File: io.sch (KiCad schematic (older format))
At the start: 2 parts

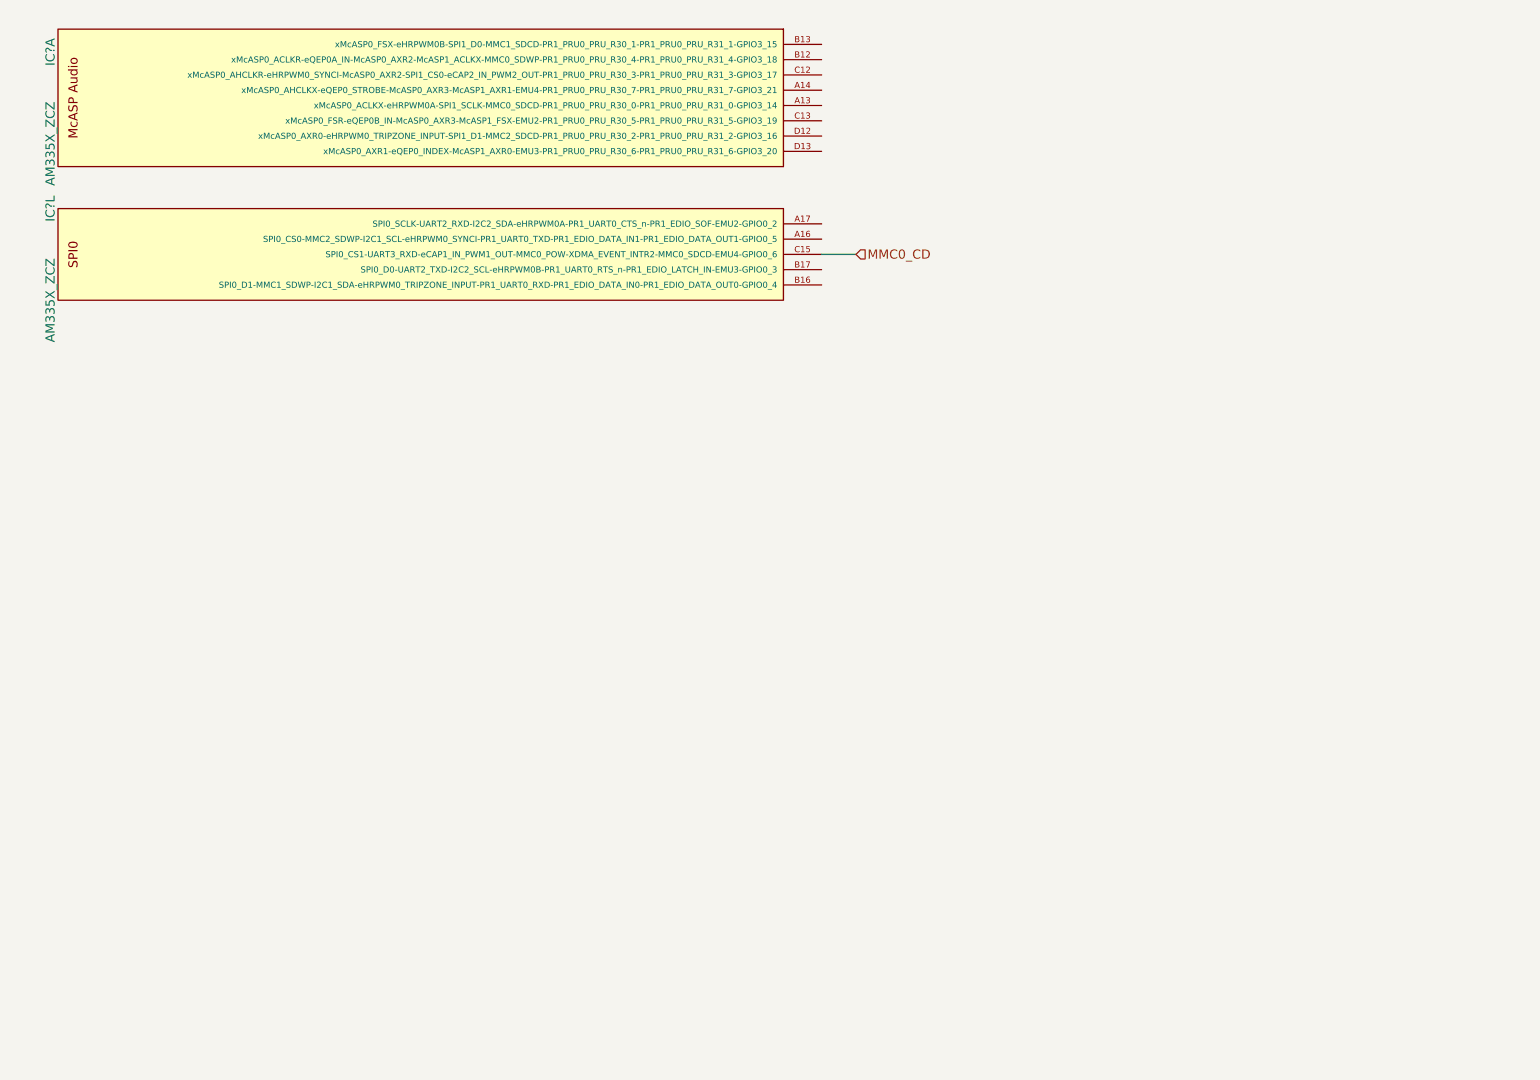
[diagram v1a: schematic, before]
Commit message: hierarchical sheets defined
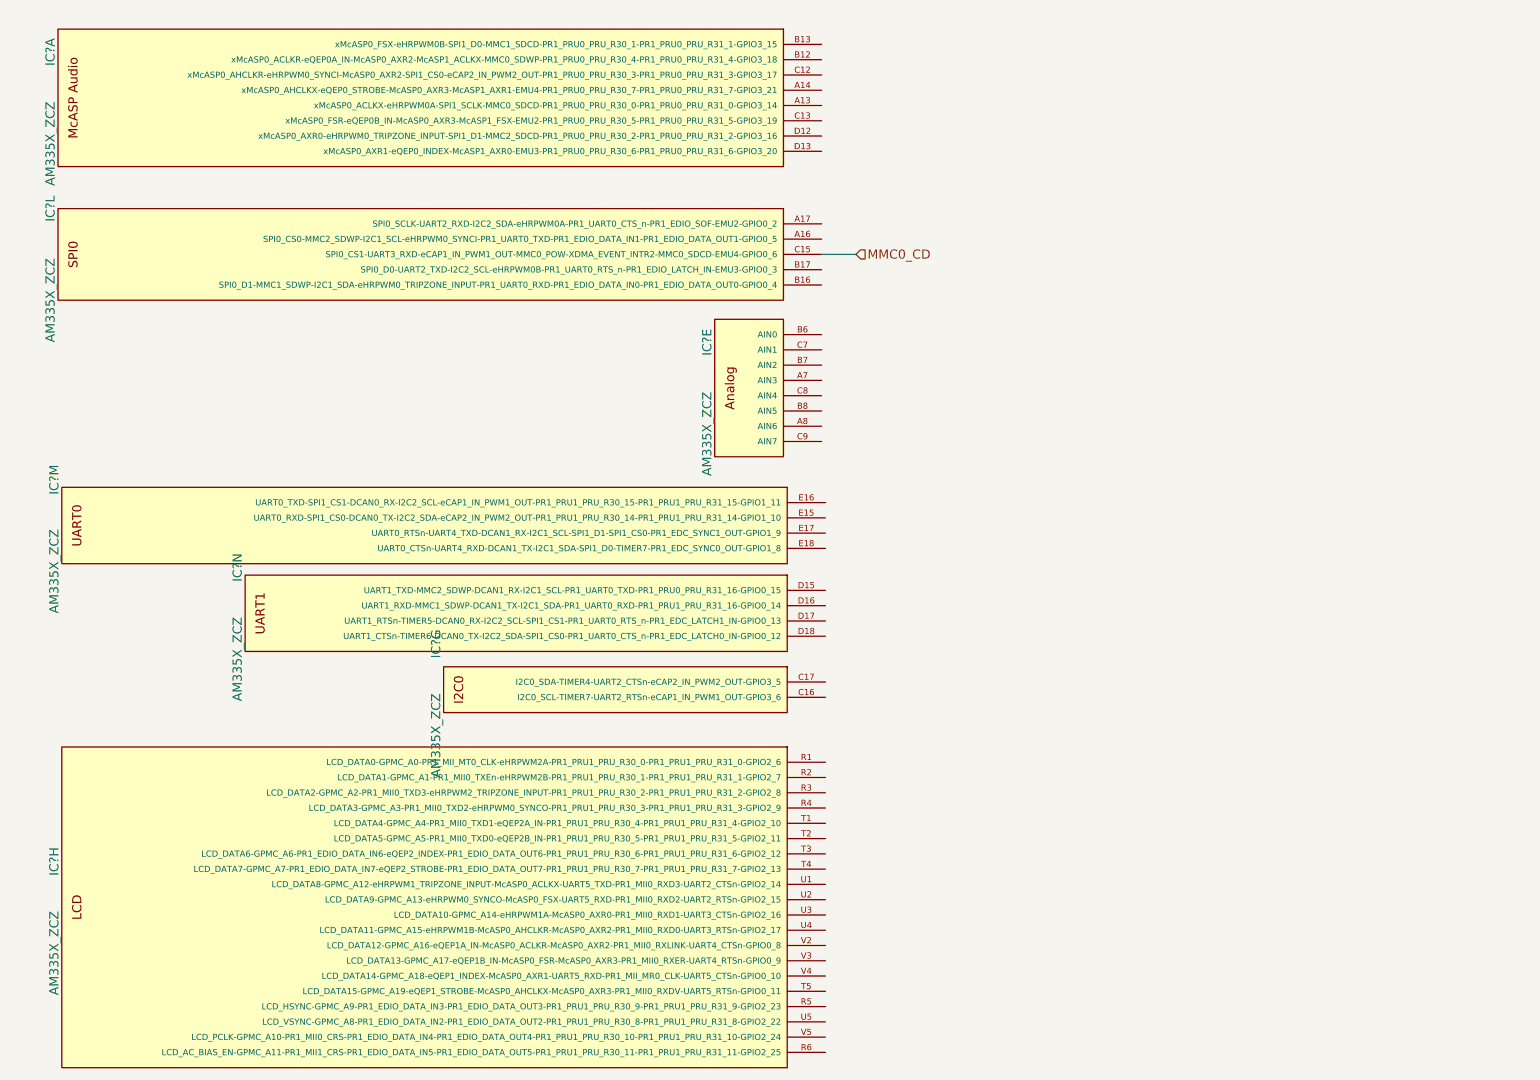
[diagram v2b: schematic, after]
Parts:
- added IC? (x5): AM335X_ZCZ, symbol AM335X_ZCZ
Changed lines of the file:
@@
 $Descr A4 11693 8268
 encoding utf-8
-Sheet 4 8
+Sheet 4 9
 Title ""
 Date ""
@@
 Text HLabel 5900 2075 2    60   Input ~ 0
 MMC0_CD
+$Comp
+L AM335X_ZCZ IC?
+U 5 1 58AD08D3
+P 4975 2950
+AR Path="/58AD08D3" Ref="IC?"  Part="5"
+AR Path="/589C7F89/58AD08D3" Ref="IC?"  Part="5"
+F 0 "IC?" V 4925 3250 60  0000 C CNN
+F 1 "AM335X_ZCZ" V 4925 2650 60  0000 C CNN
+F 2 "" H 4975 2950 60  0001 C CNN
+F 3 "" H 4975 2950 60  0001 C CNN
+	5    4975 2950
+	1    0    0    -1
+$EndComp
+$Comp
+L AM335X_ZCZ IC?
+U 13 1 58AD1F79
+P 700 3850
+F 0 "IC?" V 650 4150 60  0000 C CNN
+F 1 "AM335X_ZCZ" V 650 3550 60  0000 C CNN
+F 2 "" H 700 3850 60  0001 C CNN
+F 3 "" H 700 3850 60  0001 C CNN
+	13   700  3850
+	1    0    0    -1
+$EndComp
+$Comp
+L AM335X_ZCZ IC?
+U 14 1 58AD203C
+P 1900 4425
+F 0 "IC?" V 1850 4725 60  0000 C CNN
+F 1 "AM335X_ZCZ" V 1850 4125 60  0000 C CNN
+F 2 "" H 1900 4425 60  0001 C CNN
+F 3 "" H 1900 4425 60  0001 C CNN
+	14   1900 4425
+	1    0    0    -1
+$EndComp
+$Comp
+L AM335X_ZCZ IC?
+U 7 1 58AD3B53
+P 3200 4925
+AR Path="/58AD3B53" Ref="IC?"  Part="7"
+AR Path="/589C7F89/58AD3B53" Ref="IC?"  Part="7"
+F 0 "IC?" V 3150 5225 60  0000 C CNN
+F 1 "AM335X_ZCZ" V 3150 4625 60  0000 C CNN
+F 2 "" H 3200 4925 60  0001 C CNN
+F 3 "" H 3200 4925 60  0001 C CNN
+	7    3200 4925
+	1    0    0    -1
+$EndComp
+$Comp
+L AM335X_ZCZ IC?
+U 8 1 58AD6075
+P 700 6350
+AR Path="/58AD6075" Ref="IC?"  Part="8"
+AR Path="/589C7F89/58AD6075" Ref="IC?"  Part="8"
+F 0 "IC?" V 650 6650 60  0000 C CNN
+F 1 "AM335X_ZCZ" V 650 6050 60  0000 C CNN
+F 2 "" H 700 6350 60  0001 C CNN
+F 3 "" H 700 6350 60  0001 C CNN
+	8    700  6350
+	1    0    0    -1
+$EndComp
 $EndSCHEMATC

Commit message: wifi bt done
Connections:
- net GPIO3_20: now reaches IC?.D13 (xMcASP0_AXR1-eQEP0_INDEX-McASP1_AXR0-EMU3-PR1_PRU0_PRU_R30_6-PR1_PRU0_PRU_R31_6-GPIO3_20)
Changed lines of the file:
@@
 LIBS:tps2065cdgn
 LIBS:74lvc1g07dck
+LIBS:wl1835modgbmoct
 LIBS:mateboard-cache
 EELAYER 25 0
@@
 	1    0    0    -1
 $EndComp
+Wire Wire Line
+	5675 1400 5900 1400
+Text HLabel 5900 1400 2    60   BiDi ~ 0
+GPIO3_20
 $EndSCHEMATC

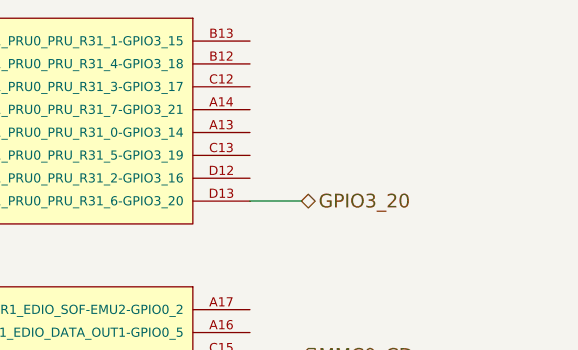
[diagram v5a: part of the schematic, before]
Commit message: id eeprom
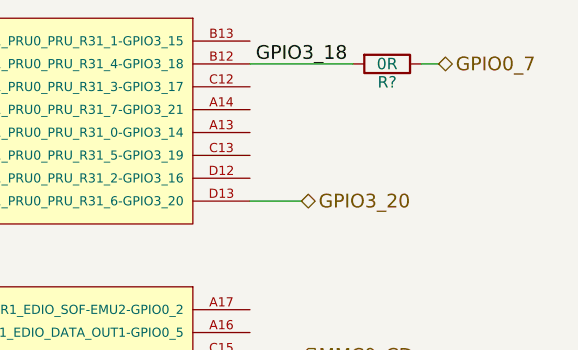
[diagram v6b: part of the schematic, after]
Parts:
- added R?: 0R, symbol R
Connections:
- net GPIO3_18: now reaches IC?.B12 (xMcASP0_ACLKR-eQEP0A_IN-McASP0_AXR2-McASP1_ACLKX-MMC0_SDWP-PR1_PRU0_PRU_R30_4-PR1_PRU0_PRU_R31_4-GPIO3_18)
- net GPIO3_18: now also R?.2
- new net GPIO0_7: R?.1
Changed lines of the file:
@@
 Text HLabel 5900 1400 2    60   BiDi ~ 0
 GPIO3_20
+Wire Wire Line
+	5675 800  6125 800
+Text Label 5700 800  0    60   ~ 0
+GPIO3_18
+$Comp
+L R R?
+U 1 1 58B968BF
+P 6275 800
+F 0 "R?" V 6355 800 50  0000 C CNN
+F 1 "0R" V 6275 800 50  0000 C CNN
+F 2 "" V 6205 800 50  0001 C CNN
+F 3 "" H 6275 800 50  0001 C CNN
+	1    6275 800
+	0    1    1    0
+$EndComp
+Wire Wire Line
+	6425 800  6500 800
+Text HLabel 6500 800  2    60   BiDi ~ 0
+GPIO0_7
 $EndSCHEMATC

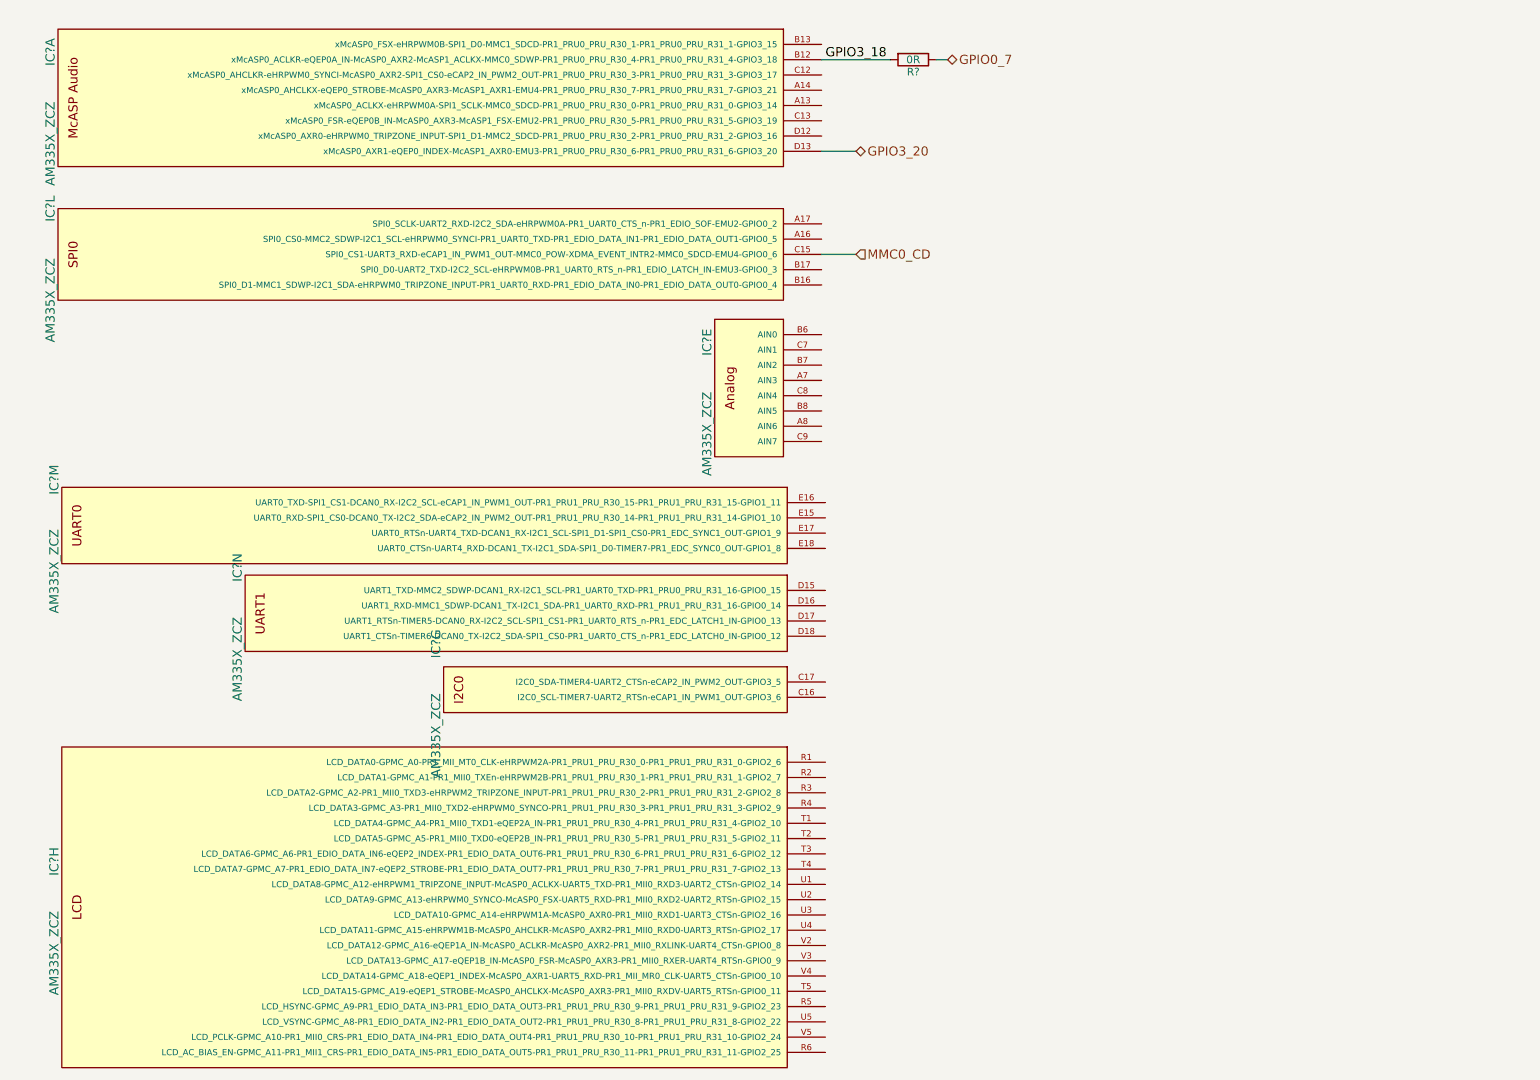
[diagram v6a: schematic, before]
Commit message: gpio and boot config
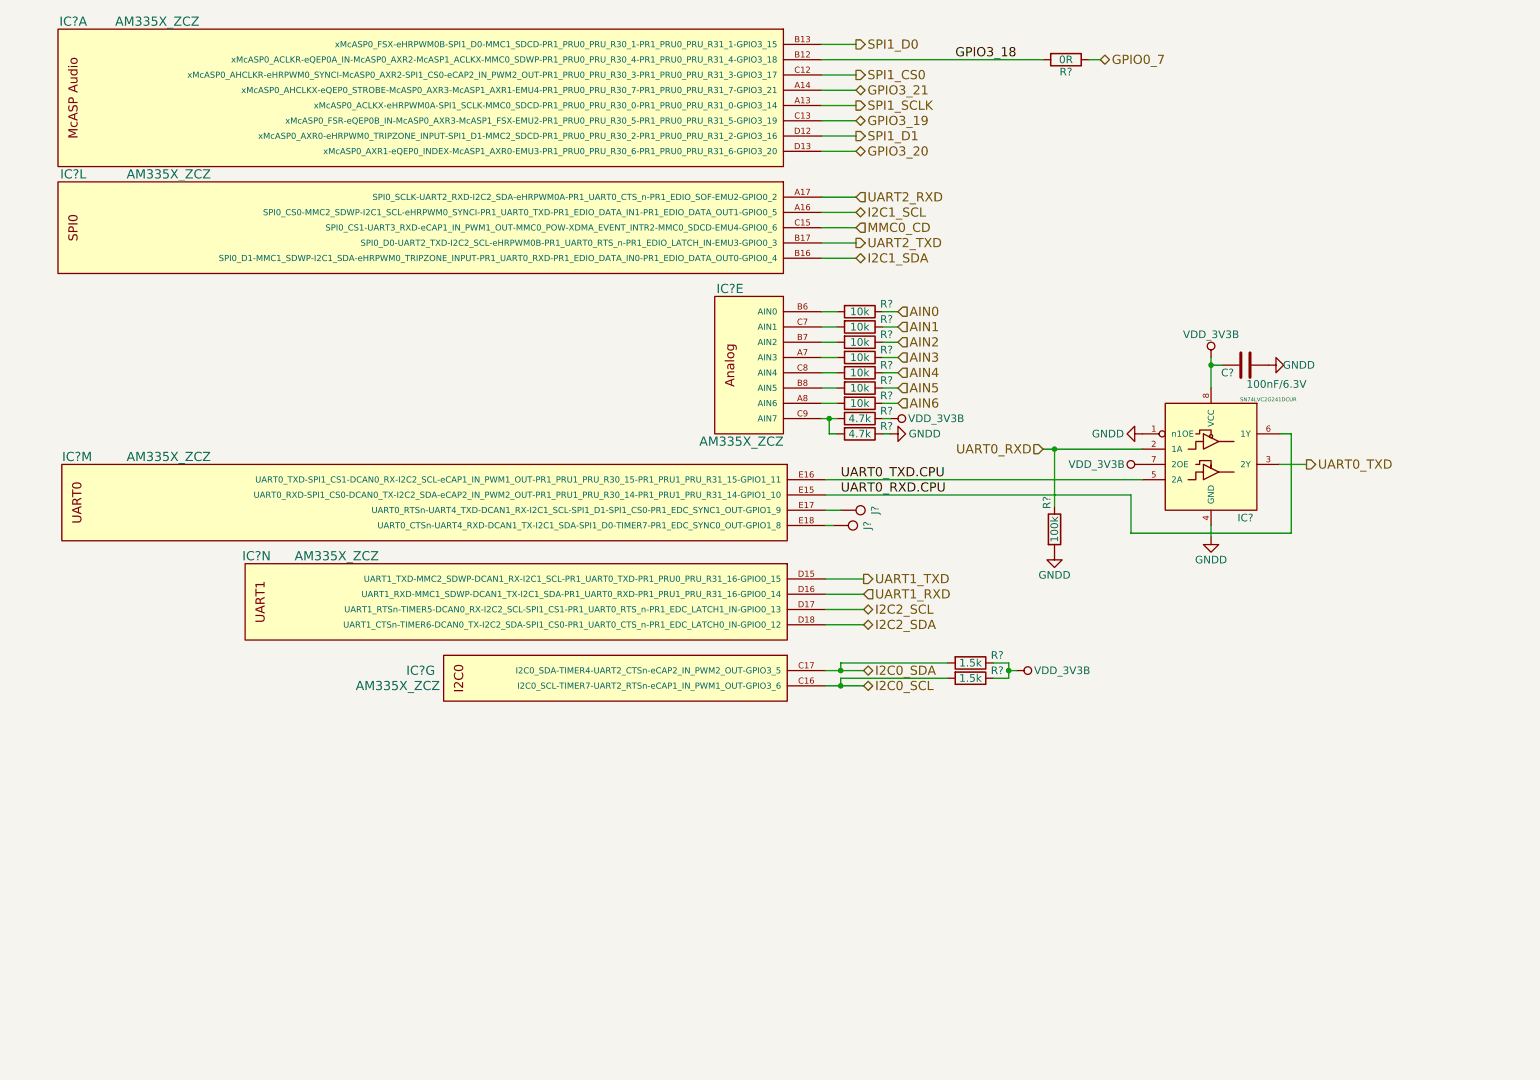
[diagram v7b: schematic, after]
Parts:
- removed IC?: AM335X_ZCZ, symbol AM335X_ZCZ
- added C?: 100nF/6.3V, symbol C
- added IC?: SN74LVC2G241DCUR, symbol LOGIC-2G125_Dual_3ST_NonInv_Buffer
- added J? (x2): TEST_1P, symbol TEST_1P
- added R? (x2): 1.5k, symbol R
- added R? (x2): 4.7k, symbol R
- added R? (x7): 10k, symbol R
- added R?: 100k, symbol R
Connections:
- net SPI1_SCLK: now reaches IC?.A13 (xMcASP0_ACLKX-eHRPWM0A-SPI1_SCLK-MMC0_SDCD-PR1_PRU0_PRU_R30_0-PR1_PRU0_PRU_R31_0-GPIO3_14)
- net GPIO3_21: now reaches IC?.A14 (xMcASP0_AHCLKX-eQEP0_STROBE-McASP0_AXR3-McASP1_AXR1-EMU4-PR1_PRU0_PRU_R30_7-PR1_PRU0_PRU_R31_7-GPIO3_21)
- net SPI1_D0: now reaches IC?.B13 (xMcASP0_FSX-eHRPWM0B-SPI1_D0-MMC1_SDCD-PR1_PRU0_PRU_R30_1-PR1_PRU0_PRU_R31_1-GPIO3_15)
- net SPI1_CS0: now reaches IC?.C12 (xMcASP0_AHCLKR-eHRPWM0_SYNCI-McASP0_AXR2-SPI1_CS0-eCAP2_IN_PWM2_OUT-PR1_PRU0_PRU_R30_3-PR1_PRU0_PRU_R31_3-GPIO3_17)
- net GPIO3_19: now reaches IC?.C13 (xMcASP0_FSR-eQEP0B_IN-McASP0_AXR3-McASP1_FSX-EMU2-PR1_PRU0_PRU_R30_5-PR1_PRU0_PRU_R31_5-GPIO3_19)
- net SPI1_D1: now reaches IC?.D12 (xMcASP0_AXR0-eHRPWM0_TRIPZONE_INPUT-SPI1_D1-MMC2_SDCD-PR1_PRU0_PRU_R30_2-PR1_PRU0_PRU_R31_2-GPIO3_16)
- net at IC?.A7 (AIN3): now also R?.2
- net at IC?.A8 (AIN6): now also R?.2
- net at IC?.B6 (AIN0): now also R?.2
- net at IC?.B7 (AIN2): now also R?.2
- net at IC?.B8 (AIN5): now also R?.2
- net at IC?.C7 (AIN1): now also R?.2
- net at IC?.C8 (AIN4): now also R?.2
- net at IC?.C9 (AIN7): now also R?.2, R?.2
- net UART0_RXD.CPU: now reaches IC?.E15 (UART0_RXD-SPI1_CS0-DCAN0_TX-I2C2_SDA-eCAP2_IN_PWM2_OUT-PR1_PRU1_PRU_R30_14-PR1_PRU1_PRU_R31_14-GPIO1_10)
- net UART0_RXD.CPU: now also IC?.6 (1Y)
- net UART0_TXD.CPU: now reaches IC?.E16 (UART0_TXD-SPI1_CS1-DCAN0_RX-I2C2_SCL-eCAP1_IN_PWM1_OUT-PR1_PRU1_PRU_R30_15-PR1_PRU1_PRU_R31_15-GPIO1_11)
- net UART0_TXD.CPU: now also IC?.5 (2A)
- net at IC?.E17 (UART0_RTSn-UART4_TXD-DCAN1_RX-I2C1_SCL-SPI1_D1-SPI1_CS0-PR1_EDC_SYNC1_OUT-GPIO1_9): now also J?.1
- net at IC?.E18 (UART0_CTSn-UART4_RXD-DCAN1_TX-I2C1_SDA-SPI1_D0-TIMER7-PR1_EDC_SYNC0_OUT-GPIO1_8): now also J?.1
- net UART1_TXD: now reaches IC?.D15 (UART1_TXD-MMC2_SDWP-DCAN1_RX-I2C1_SCL-PR1_UART0_TXD-PR1_PRU0_PRU_R31_16-GPIO0_15)
- net UART1_RXD: now reaches IC?.D16 (UART1_RXD-MMC1_SDWP-DCAN1_TX-I2C1_SDA-PR1_UART0_RXD-PR1_PRU1_PRU_R31_16-GPIO0_14)
- net I2C2_SCL: now reaches IC?.D17 (UART1_RTSn-TIMER5-DCAN0_RX-I2C2_SCL-SPI1_CS1-PR1_UART0_RTS_n-PR1_EDC_LATCH1_IN-GPIO0_13)
- net I2C2_SDA: now reaches IC?.D18 (UART1_CTSn-TIMER6-DCAN0_TX-I2C2_SDA-SPI1_CS0-PR1_UART0_CTS_n-PR1_EDC_LATCH0_IN-GPIO0_12)
- net I2C0_SCL: now reaches IC?.C16 (I2C0_SCL-TIMER7-UART2_RTSn-eCAP1_IN_PWM1_OUT-GPIO3_6)
- net I2C0_SCL: now also R?.2
- net I2C0_SDA: now reaches IC?.C17 (I2C0_SDA-TIMER4-UART2_CTSn-eCAP2_IN_PWM2_OUT-GPIO3_5)
- net I2C0_SDA: now also R?.2
- net I2C1_SCL: now reaches IC?.A16 (SPI0_CS0-MMC2_SDWP-I2C1_SCL-eHRPWM0_SYNCI-PR1_UART0_TXD-PR1_EDIO_DATA_IN1-PR1_EDIO_DATA_OUT1-GPIO0_5)
- net UART2_RXD: now reaches IC?.A17 (SPI0_SCLK-UART2_RXD-I2C2_SDA-eHRPWM0A-PR1_UART0_CTS_n-PR1_EDIO_SOF-EMU2-GPIO0_2)
- net I2C1_SDA: now reaches IC?.B16 (SPI0_D1-MMC1_SDWP-I2C1_SDA-eHRPWM0_TRIPZONE_INPUT-PR1_UART0_RXD-PR1_EDIO_DATA_IN0-PR1_EDIO_DATA_OUT0-GPIO0_4)
- net UART2_TXD: now reaches IC?.B17 (SPI0_D0-UART2_TXD-I2C2_SCL-eHRPWM0B-PR1_UART0_RTS_n-PR1_EDIO_LATCH_IN-EMU3-GPIO0_3)
- new net AIN0: R?.1
- new net AIN1: R?.1
- new net AIN2: R?.1
- new net AIN3: R?.1
- new net AIN4: R?.1
- new net AIN5: R?.1
- new net AIN6: R?.1
- new net GNDD: C?.2, IC?.1 (n1OE), IC?.4 (GND), R?.1, R?.2
- new net UART0_RXD: IC?.2 (1A), R?.1
- new net UART0_TXD: IC?.3 (2Y)
- new net VDD_3V3B: C?.1, IC?.7 (2OE), IC?.8 (VCC), R?.1, R?.1, R?.1
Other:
- moved on the sheet: IC?E, IC?G, IC?L, IC?M, IC?N, R?
